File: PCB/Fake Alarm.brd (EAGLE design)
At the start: 20.2 x 13.6 mm, 12 parts, among them IC1 NE555DG4

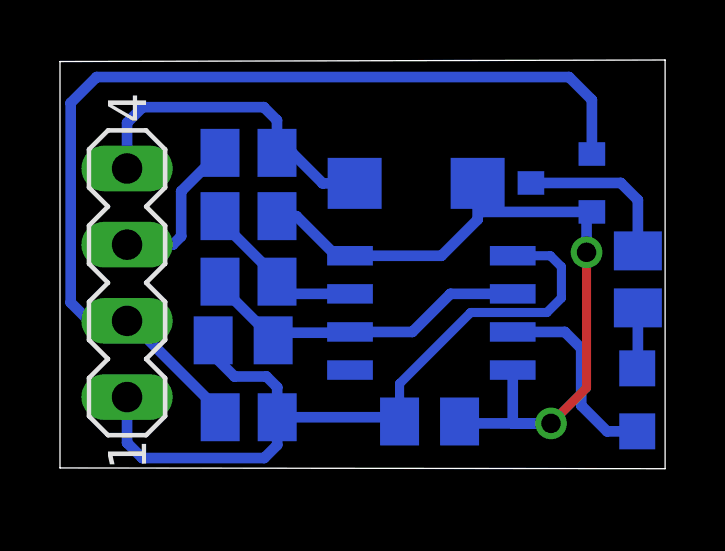
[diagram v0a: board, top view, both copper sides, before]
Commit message: New Design Fake Alarm Schematic and Layout
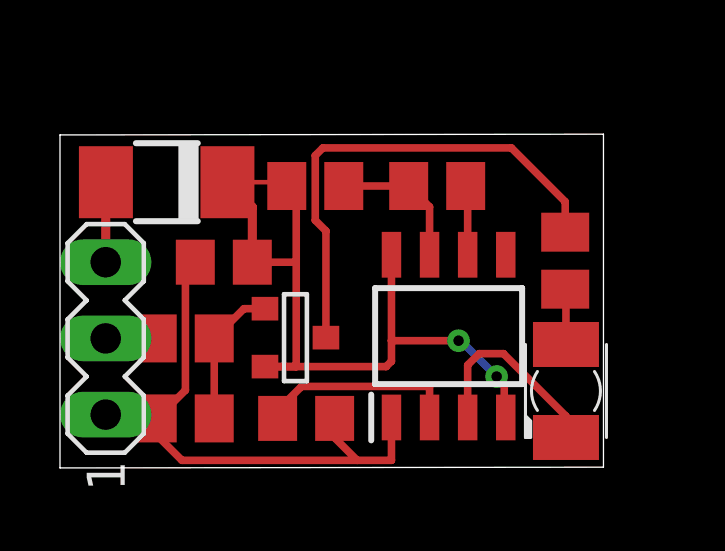
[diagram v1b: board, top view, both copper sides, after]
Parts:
- removed 1N5819: 1A-40V, diode:DO214AC
- added D1: (no value), diode:DO-214AC
- C1, C2: value 10uF -> (none); device rcl:C0805K -> rcl:C0805
- LED1: device led:CHIP-LED0805 -> led:KA-3528ASYC
- R1, R5: value 1k -> (none)
- R2: value 300k -> (none)
- R3: value 13k -> (none)
- R4: value 10k -> (none)
- SV1: device con-lstb:MA04-1 -> con-lstb:MA03-1
- moved R1 15.2 mm to (4.19, 4.32), flipped to the top, turned to 0 degrees
- moved R5 11.2 mm to (16.8, 6.91), flipped to the top, turned to 90 degrees
- moved T1 10.3 mm to (7.85, 4.32), flipped to the top
- moved R4 9.94 mm to (12.6, 9.40), flipped to the top, turned to 0 degrees
- moved R2 7.06 mm to (4.19, 1.65), flipped to the top
- moved C2 4.12 mm to (8.20, 1.65), flipped to the top, turned to 180 degrees
- moved R3 3.89 mm to (8.51, 9.40), flipped to the top
- moved C1 2.68 mm to (5.46, 6.86), flipped to the top, turned to 180 degrees
- moved LED1 2.39 mm to (16.9, 2.57), flipped to the top, turned to 270 degrees
- moved SV1 1.99 mm to (1.52, 4.32)
- moved IC1 0.96 mm to (13.0, 4.39), flipped to the top, turned to 90 degrees
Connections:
- removed net GND: C1.2, C2.2, IC1.1, R4.2, SV1.1
- removed net N$8 (its old number): R5.2, SV1.3
- new net N$10: R5.2, T1.1
- new net N$11: IC1.6, R4.2
- new net N$2: R1.1, SV1.2
- net N$1: now also D1.A, SV1.3; no longer 1N5819.C, C2.1, IC1.4, IC1.8, R2.1, T1.2
- net N$3: now also C1.2, C2.1, IC1.1, R2.1, SV1.1; no longer LED1.A, R1.1
- net N$4: now also C1.1, D1.C, IC1.4, IC1.8, R3.1, T1.2; no longer R1.2, T1.1
- net N$5: now also R1.2, R2.2; no longer R4.1, SV1.2
- net N$6: now also R3.2, R4.1; no longer R2.2, R3.1
- net N$7: now also C2.2; no longer C1.1, IC1.6, R3.2
- net N$9: now also LED1.A; no longer 1N5819.A, SV1.4
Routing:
- net N$5: track 33.2 -> 4.77 mm
- net GND: track 26.7 -> 0.00 mm
- net N$1: track 27.3 -> 2.68 mm, vias 2 -> 0
- net N$4: track 5.50 -> 27.1 mm, vias 0 -> 2
- net N$3: track 2.02 -> 19.4 mm
- net N$10: track 0.00 -> 16.4 mm
- net N$9: track 11.0 -> 1.85 mm
- net N$8 (its old number): track 5.53 -> 0.00 mm
- net N$7: track 11.3 -> 6.70 mm
- net N$11: track 0.00 -> 2.32 mm
- net N$2: track 0.00 -> 1.72 mm
- net N$6: track 6.23 -> 4.74 mm
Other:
- board size 20.2 x 13.6 mm -> 18.1 x 11.1 mm
